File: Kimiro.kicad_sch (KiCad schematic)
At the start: 27 parts, among them J2 USB_C_Left, J3 Left, J4 Right, Q1 AO3407, U1 ProMicro, U2 TP4054, U3 MS88FS3, U4 XC6220B331MR

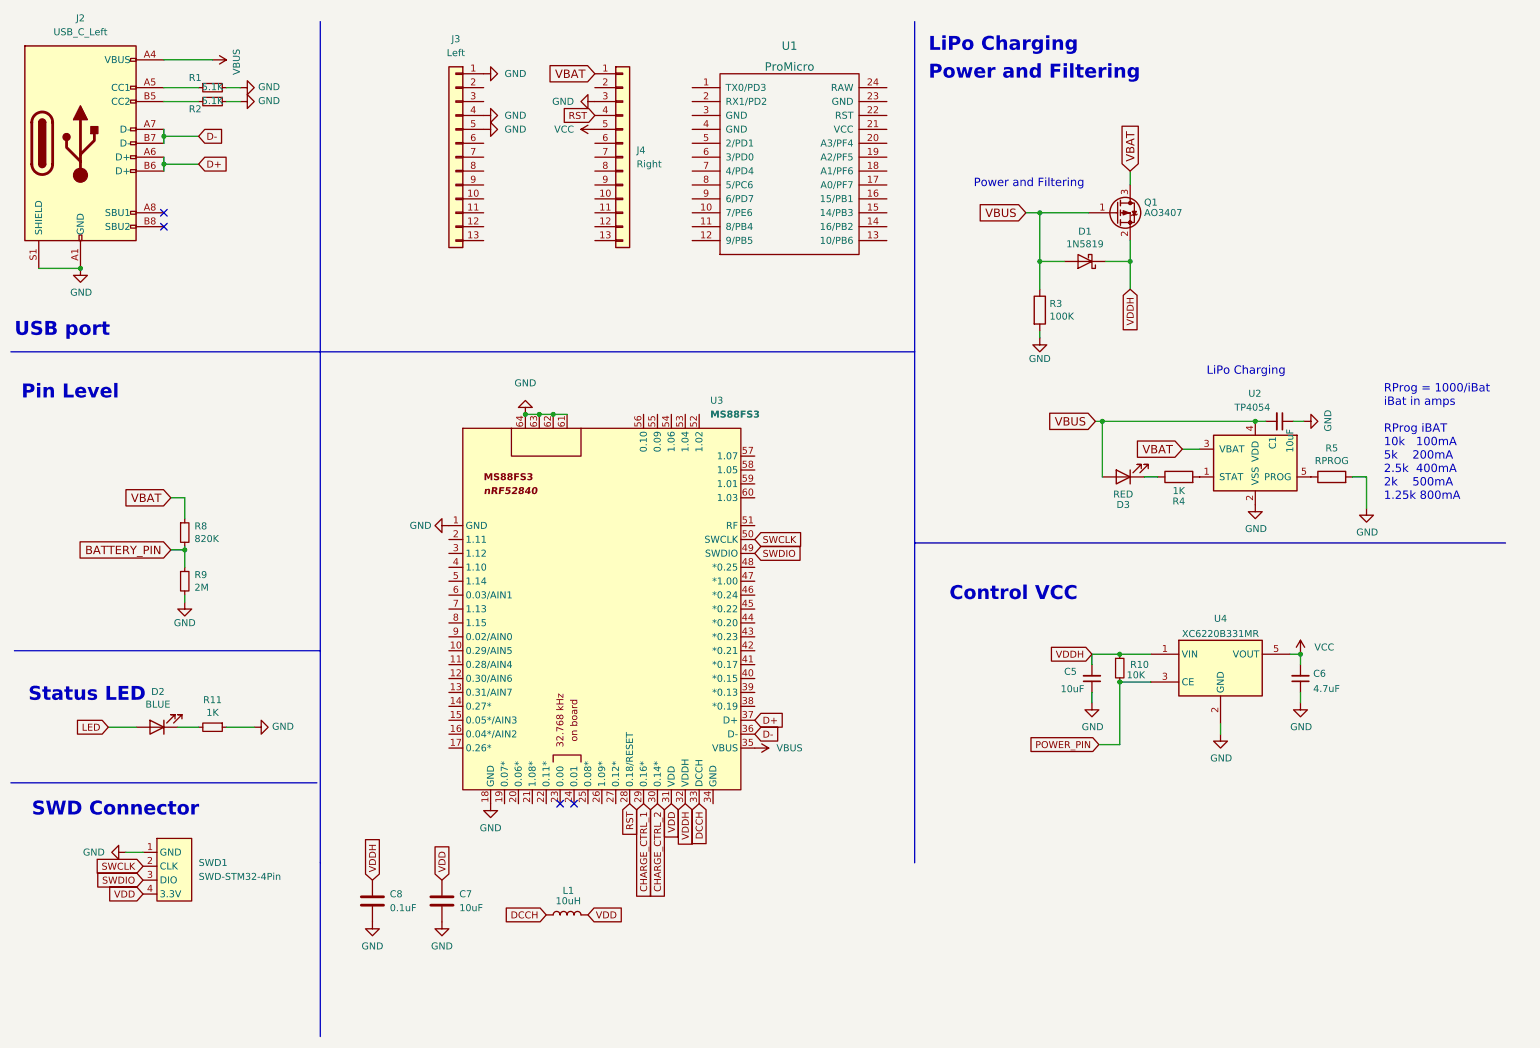
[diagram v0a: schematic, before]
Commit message: v1.0 đã hoàn thành, cần tạo proto
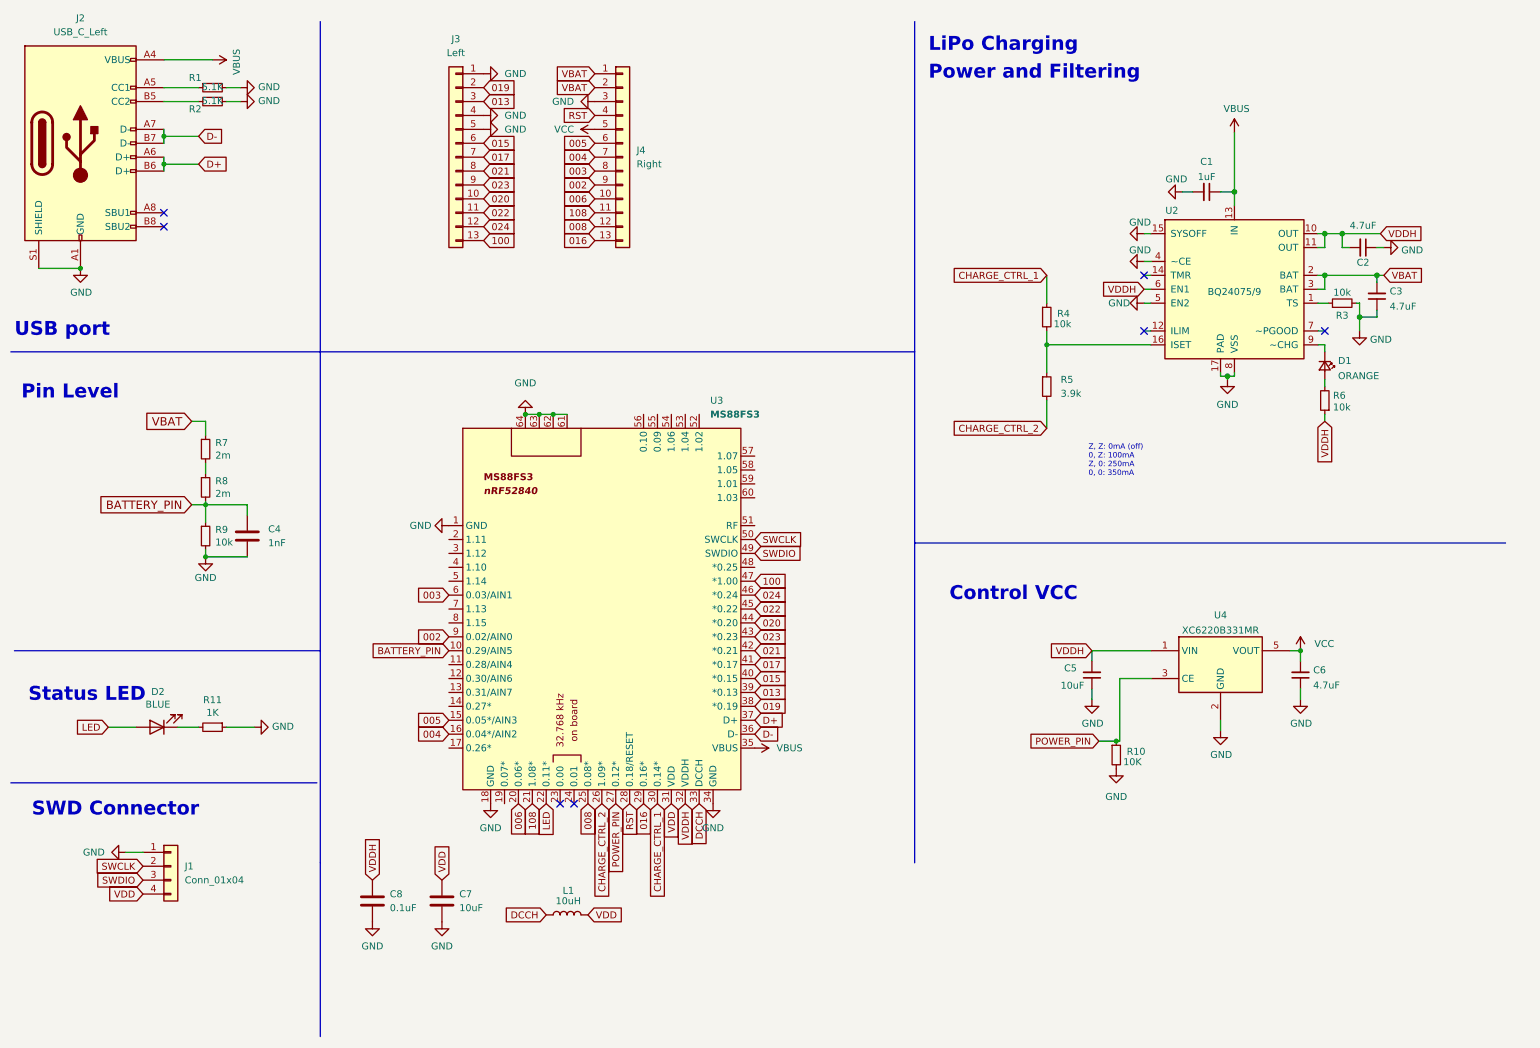
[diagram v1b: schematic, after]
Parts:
- removed D1: 1N5819, Diode_SMD:D_SOD-323F, symbol nrfmicro-rescue:MBR0520
- removed D3: RED, LED_SMD:LED_0603_1608Metric, symbol Device:LED
- removed Q1: AO3407, Package_TO_SOT_SMD:SOT-23, symbol nrfmicro-rescue:BSS83P
- removed R3: 100K, Resistor_SMD:R_0402_1005Metric, symbol nrfmicro-rescue:R
- removed R4: 1K, Resistor_SMD:R_0402_1005Metric, symbol nrfmicro-rescue:R
- removed R5: RPROG, Resistor_SMD:R_0402_1005Metric, symbol nrfmicro-rescue:R
- removed SWD1: SWD-STM32-4Pin, Sakura-library:Conn_1x04_P2.54mm, symbol keni242:SWD-STM32-4Pin
- removed U1: ProMicro, symbol keebio:ProMicro
- removed U2: TP4054, Package_TO_SOT_SMD:SOT-23-5, symbol Battery_Management:MCP73832-2-OT
- added C2, C3: 4.7uF, Capacitor_SMD:C_0402_1005Metric, symbol Device:C_Small
- added C4: 1nF, Capacitor_SMD:C_0402_1005Metric, symbol Device:C
- added D1: ORANGE, LED_SMD:LED_0603_1608Metric, symbol Device:LED_Small
- added J1: Conn_01x04, Kimiro-library:Conn_1x04_P2.54mm, symbol Connector_Generic:Conn_01x04
- added R3, R4, R6: 10k, Resistor_SMD:R_0402_1005Metric, symbol Device:R_Small
- added R5: 3.9k, Resistor_SMD:R_0402_1005Metric, symbol Device:R_Small
- added R7: 2m, Resistor_SMD:R_0402_1005Metric, symbol Device:R_Small
- added U2: BQ24075/9, Package_DFN_QFN:VQFN-16-1EP_3x3mm_P0.5mm_EP1.6x1.6mm_ThermalVias, symbol Battery_Management:BQ24075
- C1: value 10uF -> 1uF; Digikey (none) -> 1276-1067-1-ND; JLC Part C19702 -> C52923; LCSC Part C19702 -> C52923; Manufacturer Part CL10A106KP8NNNC -> CL05A105KO5NNNC
- J3, J4: footprint Sakura-library:Conn_1x13_P2.54mm -> Kimiro-library:Conn_1x13_P2.54mm
- R1, R2: footprint Capacitor_SMD:C_0402_1005Metric -> Resistor_SMD:R_0402_1005Metric
- R8: value 820K -> 2m
- R9: value 2M -> 10k
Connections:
- net BATTERY_PIN: now also U3.10 (0.29/AIN5), C4.1
- net CHARGE_CTRL_1: now also U3.30 (0.14*), R4.1; no longer U3.29 (0.16*)
- net CHARGE_CTRL_2: now also U3.26 (1.09*), R5.2; no longer U3.30 (0.14*)
- net GND: now also C1.2, R10.2, U3.34 (GND), C2.1, C3.1, C4.2, J1.1 (Pin_1), R3.2, U2.15 (SYSOFF), U2.17 (PAD), U2.4 (~CE), U2.5 (EN2), U2.8 (VSS); no longer C1.1
- net LED: now also U3.22 (0.11*)
- net POWER_PIN: now also R10.1, U3.27 (0.12*); no longer R10.2
- net SWCLK: now also J1.2 (Pin_2)
- net SWDIO: now also J1.3 (Pin_3)
- net VBAT: now also J4.2 (Pin_2), C3.2, R7.1, U2.2 (BAT), U2.3 (BAT); no longer R8.1
- net VBUS: now also C1.1, U2.13 (IN); no longer C1.2
- net VDD: now also J1.4 (Pin_4)
- net VDDH: now also C2.2, R6.1, U2.10 (OUT), U2.11 (OUT), U2.6 (EN1); no longer R10.1
- net 020: now reaches J3.10 (Pin_10)
- net 020: now also U3.44 (*0.20)
- net 022: now reaches J3.11 (Pin_11)
- net 022: now also U3.45 (*0.22)
- net 024: now reaches J3.12 (Pin_12)
- net 024: now also U3.46 (*0.24)
- net 100: now reaches J3.13 (Pin_13)
- net 100: now also U3.47 (*1.00)
- net 019: now reaches J3.2 (Pin_2)
- net 019: now also U3.38 (*0.19)
- net 013: now reaches J3.3 (Pin_3)
- net 013: now also U3.39 (*0.13)
- net 015: now reaches J3.6 (Pin_6)
- net 015: now also U3.40 (*0.15)
- net 017: now reaches J3.7 (Pin_7)
- net 017: now also U3.41 (*0.17)
- net 021: now reaches J3.8 (Pin_8)
- net 021: now also U3.42 (*0.21)
- net 023: now reaches J3.9 (Pin_9)
- net 023: now also U3.43 (*0.23)
- net 005: now reaches U3.15 (0.05*/AIN3)
- net 005: now also J4.6 (Pin_6)
- net 004: now reaches U3.16 (0.04*/AIN2)
- net 004: now also J4.7 (Pin_7)
- net 006: now reaches U3.20 (0.06*)
- net 006: now also J4.10 (Pin_10)
- net 108: now reaches U3.21 (1.08*)
- net 108: now also J4.11 (Pin_11)
- net 008: now reaches U3.25 (0.08*)
- net 008: now also J4.12 (Pin_12)
- net 003: now reaches U3.6 (0.03/AIN1)
- net 003: now also J4.8 (Pin_8)
- net 002: now reaches U3.9 (0.02/AIN0)
- net 002: now also J4.9 (Pin_9)
- net 016: now reaches J4.13 (Pin_13)
- net 016: now also U3.29 (0.16*)
- new net: R3.1, U2.1 (TS)
- new net: D1.1 (K), U2.9 (~CHG)
- new net: D1.2 (A), R6.2
- new net: R7.2, R8.1
- new net: R4.2, R5.1, U2.16 (ISET)
- no-connect marks 4 -> 7
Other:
- note added: "Z, Z: 0mA (off) 0, Z: 100mA Z, 0: 250mA 0, 0: 350mA"
- note removed: "RProg = 1000/iBat iBat in amps RProg iBAT 10k 100mA 5k 200mA 2.5k 400mA 2k 500mA 1.25k 800mA"
- moved on the sheet: C5, C6, R10, U4

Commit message: 10:42 30/03/2022
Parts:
- U2: footprint Package_DFN_QFN:VQFN-16-1EP_3x3mm_P0.5mm_EP1.6x1.6mm_ThermalVias -> kien242:BQ24075
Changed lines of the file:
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@@
     (property "Reference" "U2" (id 0) (at 224.79 47.8494 0))
     (property "Value" "BQ24075/9" (id 1) (at 236.22 62.6895 0))
-    (property "Footprint" "Package_DFN_QFN:VQFN-16-1EP_3x3mm_P0.5mm_EP1.6x1.6mm_ThermalVias" (id 2) (at 242.57 76.2 0)
+    (property "Footprint" "kien242:BQ24075" (id 2) (at 242.57 76.2 0)
       (effects (font (size 1.27 1.27)) (justify left) hide)
     )
@@
     )
     (path "/665122c6-5978-4523-b37b-0e50a2a66731"
-      (reference "U2") (unit 1) (value "BQ24075/9") (footprint "Package_DFN_QFN:VQFN-16-1EP_3x3mm_P0.5mm_EP1.6x1.6mm_ThermalVias")
+      (reference "U2") (unit 1) (value "BQ24075/9") (footprint "kien242:BQ24075")
     )
     (path "/599cca88-87e6-4132-8254-2ef0bbd3c10d"

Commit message: cập nhật 12:21 08/06/2022
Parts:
- R4: value 10k -> 1.87k
- R5: value 3.9k -> 4.7k
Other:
- note added: "Z, Z: 0mA (off) 0, Z: 500mA Z, 0: 200mA 0, 0: 350mA(???)"
- note removed: "Z, Z: 0mA (off) 0, Z: 100mA Z, 0: 250mA 0, 0: 350mA"
- moved on the sheet: R5
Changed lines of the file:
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@@
     (stroke (width 0) (type default) (color 0 0 0 0))
   )
-  (wire (pts (xy 201.93 72.39) (xy 201.93 77.47))
+  (wire (pts (xy 201.93 72.39) (xy 201.93 76.2))
     (stroke (width 0) (type default) (color 0 0 0 0))
   )
@@
     (stroke (width 0) (type default) (color 0 0 0 0))
   )
-  (wire (pts (xy 201.93 87.63) (xy 201.93 82.55))
+  (wire (pts (xy 201.93 87.63) (xy 201.93 81.28))
     (stroke (width 0) (type default) (color 0 0 0 0))
   )
@@
     (effects (font (size 2.54 2.54) (thickness 0.508) bold) (justify left bottom))
   )
-  (text "Z, Z: 0mA (off)\n0, Z: 100mA\nZ, 0: 250mA\n0, 0: 350mA"
+  (text "Z, Z: 0mA (off)\n0, Z: 500mA\nZ, 0: 200mA\n0, 0: 350mA(???)"
     (at 209.55 96.52 0)
     (effects (font (size 0.9906 0.9906)) (justify left bottom))
@@
     (pin "2")
   )
-  (symbol (lib_id "Device:R_Small") (at 201.93 80.01 0) (unit 1)
-    (in_bom yes) (on_board yes) (fields_autoplaced)
-    (property "Reference" "R5" (id 0) (at 204.47 78.7399 0)
-      (effects (font (size 1.27 1.27)) (justify left))
-    )
-    (property "Value" "3.9k" (id 1) (at 204.47 81.2799 0)
-      (effects (font (size 1.27 1.27)) (justify left))
-    )
-    (property "Footprint" "Resistor_SMD:R_0402_1005Metric" (id 2) (at 201.93 80.01 0)
-      (effects (font (size 1.27 1.27)) hide)
-    )
-    (property "Datasheet" "~" (id 3) (at 201.93 80.01 0)
-      (effects (font (size 1.27 1.27)) hide)
-    )
-    (property "LCSC Part" "C131467" (id 4) (at 201.93 80.01 0)
-      (effects (font (size 1.27 1.27)) hide)
-    )
-    (property "Manufacturer Part" "RC0402FR-073K9L" (id 5) (at 201.93 80.01 0)
-      (effects (font (size 1.27 1.27)) hide)
-    )
-    (property "JLC Part" "C51721" (id 6) (at 201.93 80.01 0)
+  (symbol (lib_id "Device:R_Small") (at 201.93 78.74 0) (unit 1)
+    (in_bom yes) (on_board yes) (fields_autoplaced)
+    (property "Reference" "R5" (id 0) (at 204.47 77.4699 0)
+      (effects (font (size 1.27 1.27)) (justify left))
+    )
+    (property "Value" "4.7k" (id 1) (at 204.47 80.0099 0)
+      (effects (font (size 1.27 1.27)) (justify left))
+    )
+    (property "Footprint" "Resistor_SMD:R_0402_1005Metric" (id 2) (at 201.93 78.74 0)
+      (effects (font (size 1.27 1.27)) hide)
+    )
+    (property "Datasheet" "~" (id 3) (at 201.93 78.74 0)
+      (effects (font (size 1.27 1.27)) hide)
+    )
+    (property "LCSC Part" "C131467" (id 4) (at 201.93 78.74 0)
+      (effects (font (size 1.27 1.27)) hide)
+    )
+    (property "Manufacturer Part" "RC0402FR-073K9L" (id 5) (at 201.93 78.74 0)
+      (effects (font (size 1.27 1.27)) hide)
+    )
+    (property "JLC Part" "C51721" (id 6) (at 201.93 78.74 0)
       (effects (font (size 1.27 1.27)) hide)
     )
@@
       (effects (font (size 1.27 1.27)) (justify left))
     )
-    (property "Value" "10k" (id 1) (at 203.2 68.58 0)
+    (property "Value" "1.87k" (id 1) (at 203.2 68.58 0)
       (effects (font (size 1.27 1.27)) (justify left))
     )
@@
     )
     (path "/6a81b739-960e-4ae8-bfd1-6cb2b5d54abd"
-      (reference "R4") (unit 1) (value "10k") (footprint "Resistor_SMD:R_0402_1005Metric")
+      (reference "R4") (unit 1) (value "1.87k") (footprint "Resistor_SMD:R_0402_1005Metric")
     )
     (path "/46189e15-73a7-47af-aa31-8f9fe5430069"
-      (reference "R5") (unit 1) (value "3.9k") (footprint "Resistor_SMD:R_0402_1005Metric")
+      (reference "R5") (unit 1) (value "4.7k") (footprint "Resistor_SMD:R_0402_1005Metric")
     )
     (path "/7d48fea1-5a07-43f0-9ab1-5fc2a66580c1"
